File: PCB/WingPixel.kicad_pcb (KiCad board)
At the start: 4 copper layers, 50.8 x 22.9 mm, 20 parts, among them J1 Barrel_Jack, J2 Screw_Terminal_01x04, J3 Conn_01x16, J4 Conn_01x12, J5 TriSolderJumper, J6 Conn_01x02, SW1 SW_Push, U1 WingPixel, U2 LSF0102DCUR

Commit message: Changing power distribution
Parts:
- moved J5 8.24 mm to (51.1, 38.9)
- moved J6 3.84 mm to (49.5, 35.3), turned to 90 degrees
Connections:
- C1 pad 1: VEXT -> VLED
- J2 pad 1: VEXT -> VLED
- J5 pad 2: VEXT -> VLED
- R1 pad 2: VEXT -> VLED
- R4 pad 2: VEXT -> VLED
- R5 pad 2: VEXT -> VLED
- U2 pad 7: VEXT -> VLED
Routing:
- net VEXT: track 54.4 -> 7.84 mm, vias 3 -> 0
- net VUSB: track 17.8 -> 2.54 mm, vias 1 -> 0
- net VLED: track 0.00 -> 12.9 mm
- net VBATT: track 6.61 -> 2.54 mm
- removed copper zone on In1.Cu, net VEXT

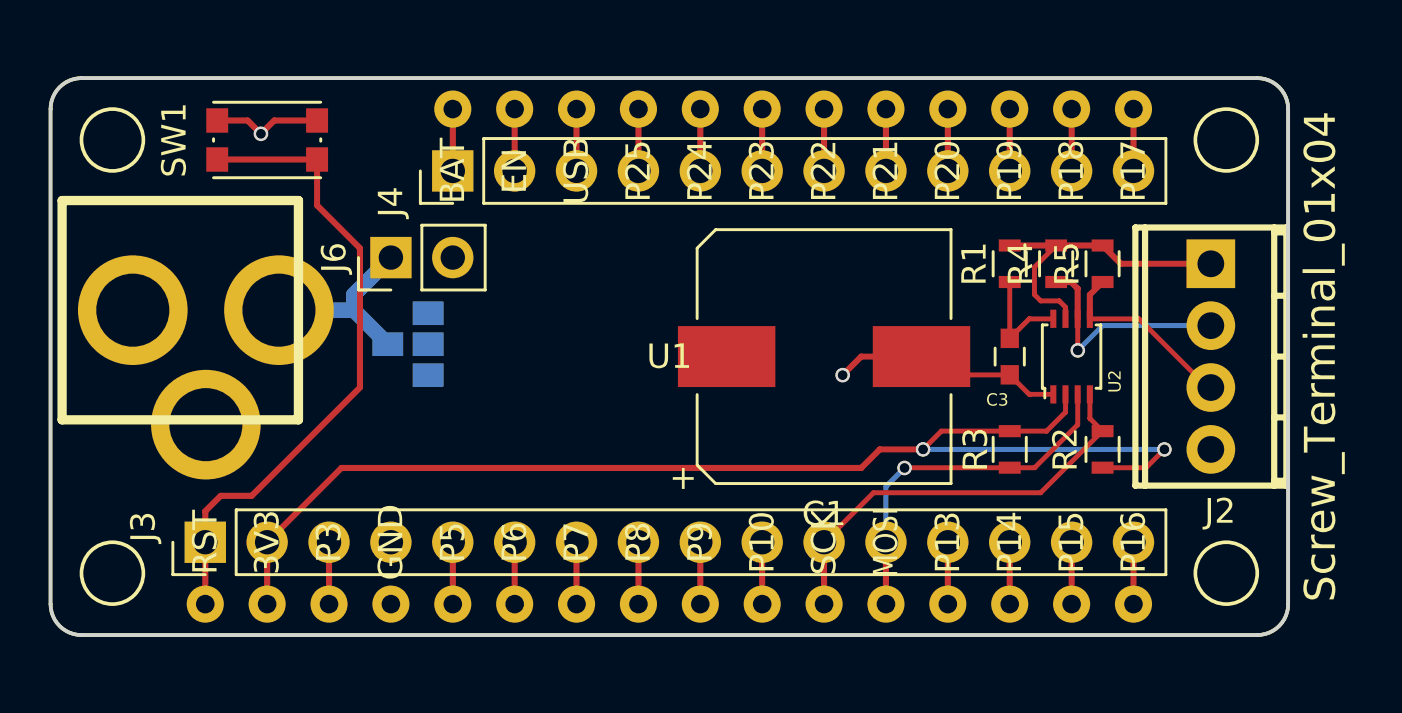
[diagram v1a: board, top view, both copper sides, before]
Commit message: Adjusted Power Distribution, defined zones
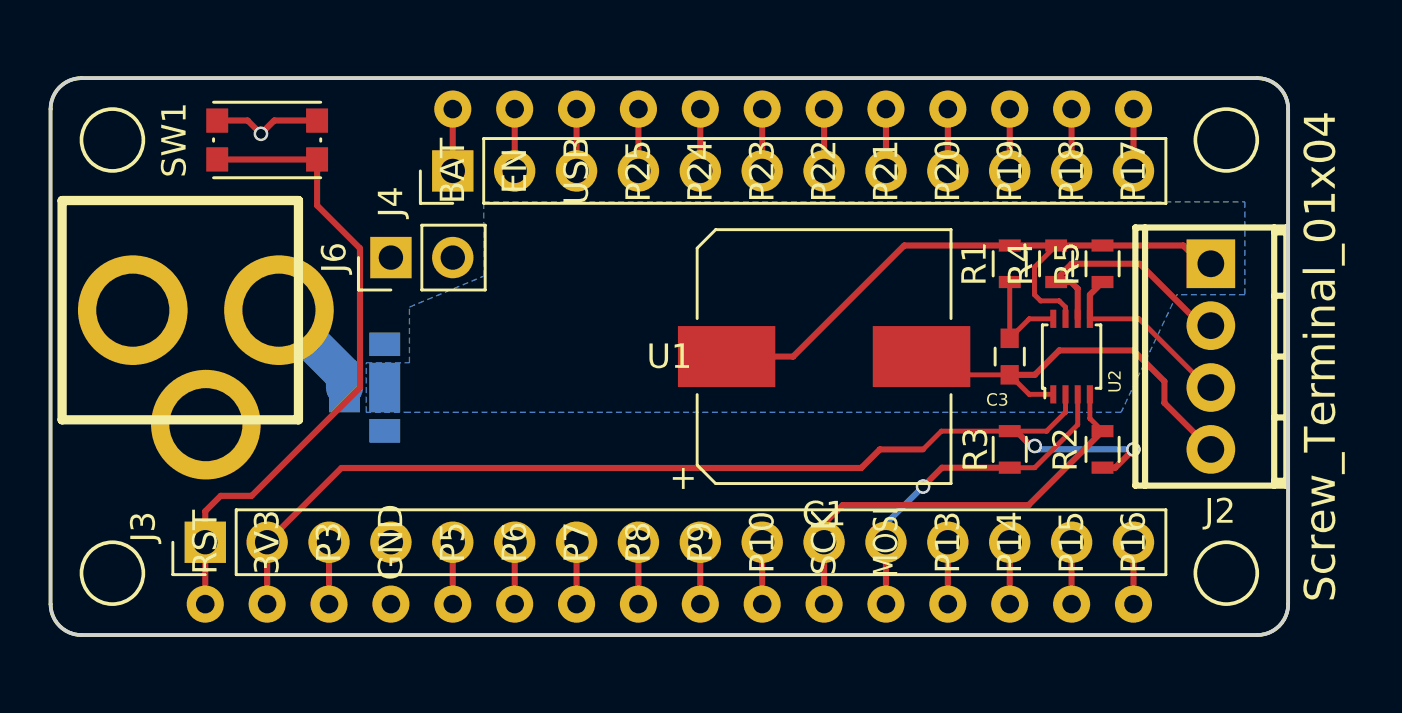
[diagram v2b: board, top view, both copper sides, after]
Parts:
- J5: footprint TriSelectSolderJumper:TriSelectSolderJumper_CutTrace -> TriSelectSolderJumper:TriSelectSolderJumper_HighCurrent
- moved J5 2.51 mm to (49.3, 40.6)
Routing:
- net GND: track 59.4 -> 39.4 mm, vias 2 -> 1
- net VLED: track 12.9 -> 26.4 mm
- net V3v3: track 51.0 -> 45.2 mm
- net VEXT: track 7.84 -> 4.29 mm
- net MOSI: track 15.0 -> 14.1 mm
- net DATA: track 9.42 -> 10.0 mm, vias 1 -> 0
- added copper zone on B.Cu, net VLED

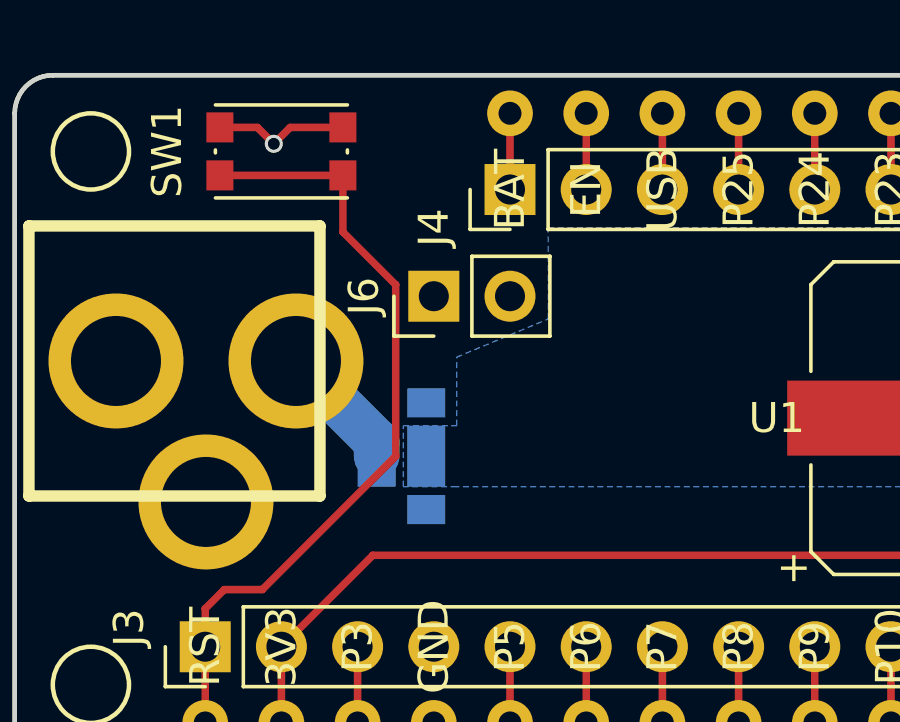
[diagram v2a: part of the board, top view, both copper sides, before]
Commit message: Connected VUSB, VBATT, Modified Zone for VEXT
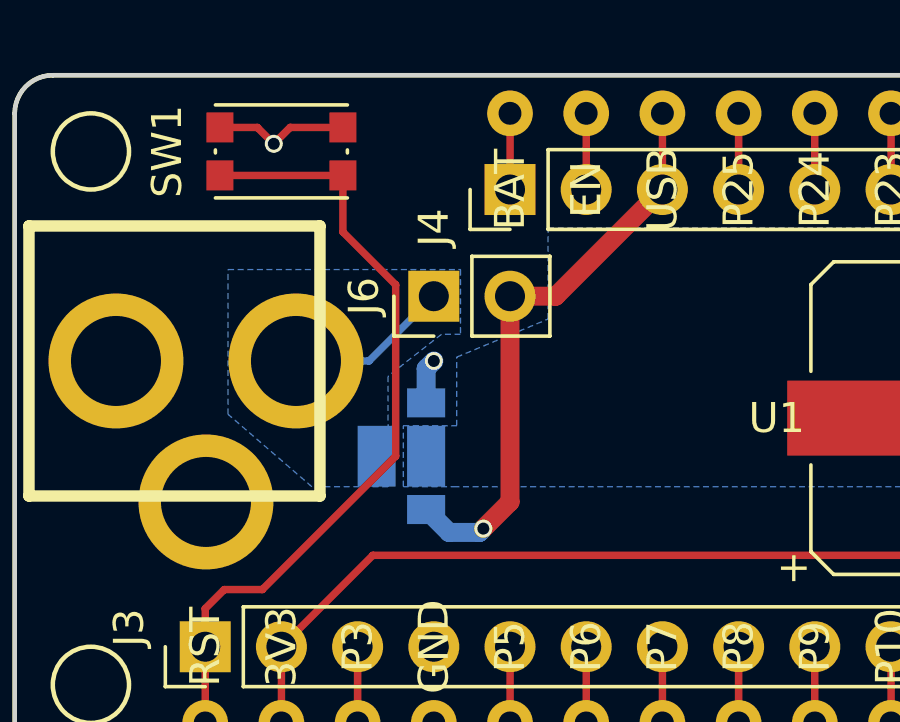
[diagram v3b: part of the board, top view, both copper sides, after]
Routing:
- net VUSB: track 2.54 -> 19.5 mm, vias 0 -> 1
- net VBATT: track 2.54 -> 13.8 mm, vias 0 -> 1
- net VEXT: track 4.29 -> 5.49 mm
- added copper zone on B.Cu, net VEXT
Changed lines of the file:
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@@
   (general
     (links 62)
-    (no_connects 5)
-    (area 35.484999 27.864999 86.435001 50.875001)
+    (no_connects 1)
+    (area 29.971429 25.695 91.948572 52.835)
     (thickness 1.6)
     (drawings 8)
-    (tracks 119)
+    (tracks 135)
     (zones 0)
     (modules 20)
@@
     (user_trace_width 0.2032)
     (user_trace_width 0.635)
-    (user_trace_width 1.524)
+    (user_trace_width 1.27)
     (trace_clearance 0.2)
-    (zone_clearance 0.381)
+    (zone_clearance 0.254)
     (zone_45_only no)
     (trace_min 0.2)
@@
   (segment (start 76.72 37.82) (end 75.73 37.82) (width 0.2032) (layer F.Cu) (net 22))
   (segment (start 75.73 37.82) (end 74.93 38.62) (width 0.2032) (layer F.Cu) (net 22))
-  (segment (start 74.93 40.12) (end 75.958 40.12) (width 0.25) (layer F.Cu) (net 23) (status 400000))
-  (segment (start 81.28 41.275) (end 83.185 43.18) (width 0.25) (layer F.Cu) (net 23) (status 800000))
+  (segment (start 74.93 40.12) (end 75.958 40.12) (width 0.25) (layer F.Cu) (net 23))
+  (segment (start 81.28 41.275) (end 83.185 43.18) (width 0.25) (layer F.Cu) (net 23))
   (segment (start 81.28 40.386) (end 81.28 41.275) (width 0.25) (layer F.Cu) (net 23))
   (segment (start 80.01 39.116) (end 81.28 40.386) (width 0.25) (layer F.Cu) (net 23))
@@
   (segment (start 76.442 42.43) (end 74.93 42.43) (width 0.2032) (layer F.Cu) (net 24))
   (segment (start 77.22 41.652) (end 76.442 42.43) (width 0.2032) (layer F.Cu) (net 24))
-  (segment (start 47.625 40.64) (end 47.625 40.15486) (width 1.524) (layer B.Cu) (net 25))
-  (segment (start 47.625 40.15486) (end 44.93514 37.465) (width 1.524) (layer B.Cu) (net 25))
+  (segment (start 44.93514 37.465) (end 47.371 37.465) (width 0.25) (layer B.Cu) (net 25))
+  (segment (start 47.371 37.465) (end 49.53 35.306) (width 0.25) (layer B.Cu) (net 25))
   (segment (start 76.835 36.31) (end 76.835 36.195) (width 0.25) (layer F.Cu) (net 26))
   (segment (start 76.835 36.195) (end 77.47 35.56) (width 0.25) (layer F.Cu) (net 26))
@@
   (segment (start 75.958 43.93) (end 74.93 43.93) (width 0.2032) (layer F.Cu) (net 30))
   (segment (start 77.72 42.168) (end 75.958 43.93) (width 0.2032) (layer F.Cu) (net 30))
+  (segment (start 52.07 31.75) (end 52.07 33.02) (width 0.635) (layer In1.Cu) (net 31))
+  (segment (start 49.276 37.719) (end 49.276 38.862) (width 0.635) (layer B.Cu) (net 31))
+  (segment (start 49.53 37.465) (end 49.276 37.719) (width 0.635) (layer B.Cu) (net 31))
+  (via (at 49.53 37.465) (size 0.6) (drill 0.4) (layers F.Cu B.Cu) (net 31))
+  (segment (start 52.324 37.465) (end 49.53 37.465) (width 0.635) (layer In1.Cu) (net 31))
+  (segment (start 53.721 36.068) (end 52.324 37.465) (width 0.635) (layer In1.Cu) (net 31))
+  (segment (start 53.721 34.671) (end 53.721 36.068) (width 0.635) (layer In1.Cu) (net 31))
+  (segment (start 52.07 33.02) (end 53.721 34.671) (width 0.635) (layer In1.Cu) (net 31))
   (segment (start 52.07 31.75) (end 52.07 29.21) (width 0.25) (layer F.Cu) (net 31))
+  (segment (start 52.07 35.306) (end 52.07 42.164) (width 0.635) (layer F.Cu) (net 32))
+  (segment (start 50.038 43.18) (end 49.276 42.418) (width 0.635) (layer B.Cu) (net 32))
+  (segment (start 51.054 43.18) (end 50.038 43.18) (width 0.635) (layer B.Cu) (net 32))
+  (segment (start 51.181 43.053) (end 51.054 43.18) (width 0.635) (layer B.Cu) (net 32))
+  (via (at 51.181 43.053) (size 0.6) (drill 0.4) (layers F.Cu B.Cu) (net 32))
+  (segment (start 52.07 42.164) (end 51.181 43.053) (width 0.635) (layer F.Cu) (net 32))
+  (segment (start 52.07 35.306) (end 53.594 35.306) (width 0.635) (layer F.Cu) (net 32))
+  (segment (start 53.594 35.306) (end 57.15 31.75) (width 0.635) (layer F.Cu) (net 32))
   (segment (start 57.15 29.21) (end 57.15 31.75) (width 0.25) (layer F.Cu) (net 32))
   (segment (start 63.31 39.37) (end 66.04 39.37) (width 0.25) (layer F.Cu) (net 33))
@@
       )
     )
+  )
+  (zone (net 25) (net_name VEXT) (layer B.Cu) (hatch edge 0.508)
+    (connect_pads (clearance 0.254))
+    (min_thickness 0.254)
+    (fill yes (arc_segments 16) (thermal_gap 0.2032) (thermal_bridge_width 1.524))
+    (polygon
+      (pts
+        (xy 50.419 36.576) (xy 49.784 36.576) (xy 48.006 37.973) (xy 48.006 41.656) (xy 45.466 41.656)
+        (xy 42.672 39.243) (xy 42.672 34.417) (xy 50.419 34.417)
+      )
+    )

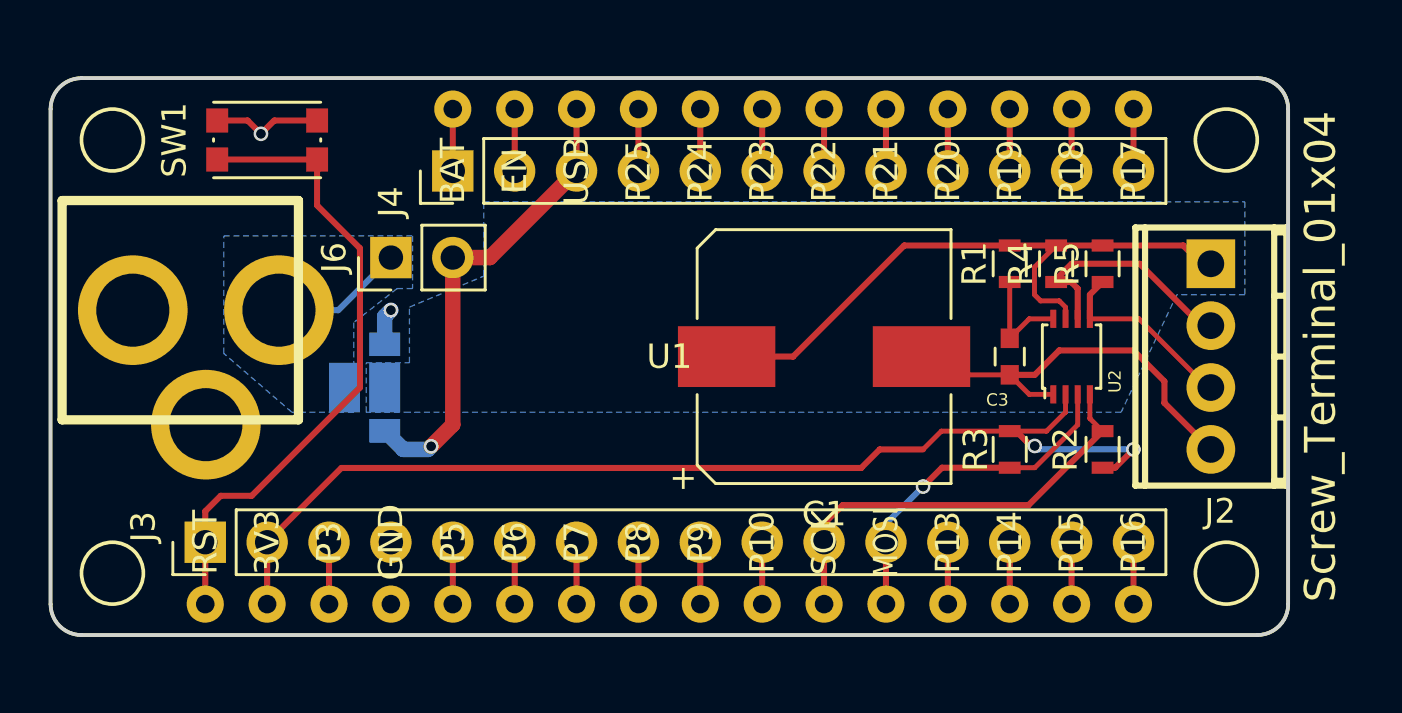
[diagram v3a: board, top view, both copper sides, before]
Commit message: Cleaned up Silk Screen, Added Labels and Logos
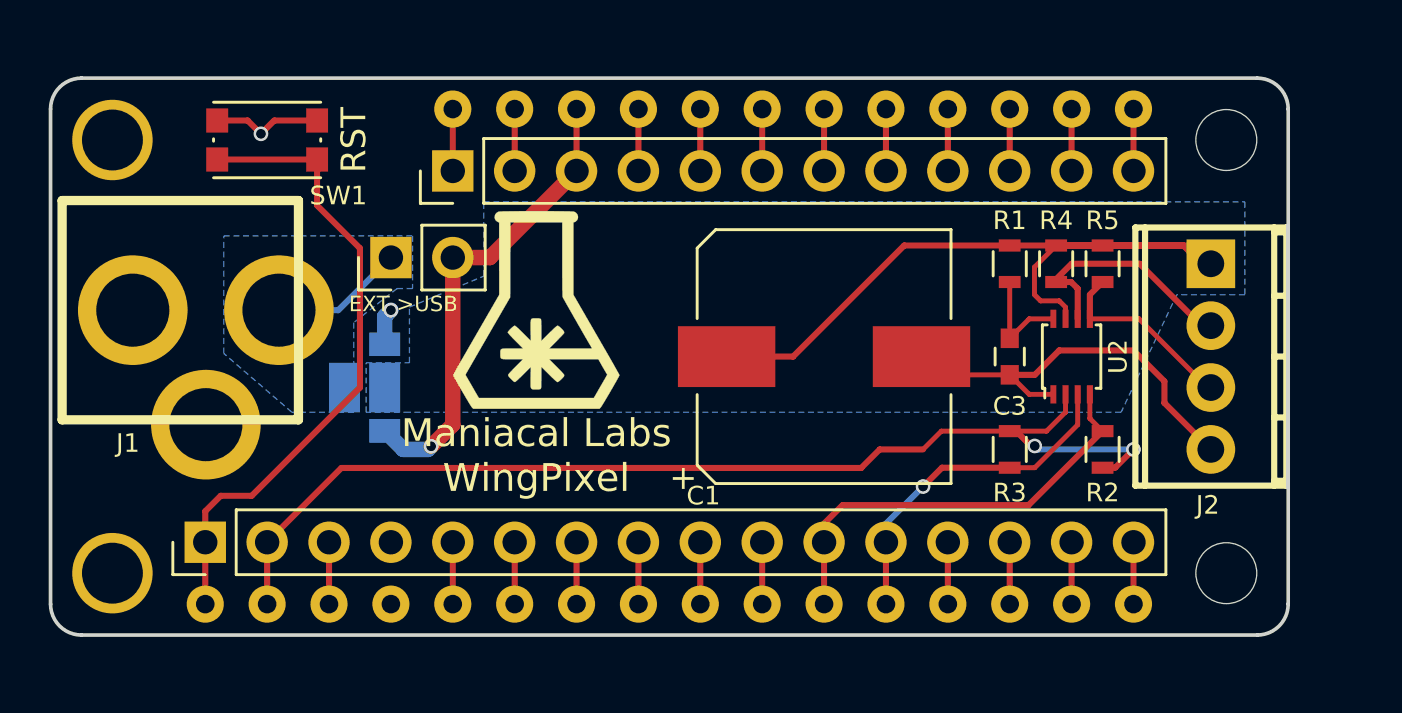
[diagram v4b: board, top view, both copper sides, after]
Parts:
- added G***: LOGO, LOGOS:logo_MLlabs_small, F.Cu at (55.5, 37.5)
- U1: footprint FeatherWing:FeatherWing -> FeatherWing:FeatherWing_NoOutline
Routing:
- net VLED: track 26.4 -> 33.1 mm
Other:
- board text added: "BAT"
- board text added: "EXT"
- board text added: "EXT >USB"
- board text added: "LED"
- board text added: "Maniacal Labs WingPixel"
- board text added: "RST"
- board text added: "USB"
- board text added: "VLED Jumper See Manual CHOOSE ONLY ONE TO POWER LEDs"

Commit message: Converted to 2-Layer board(!)
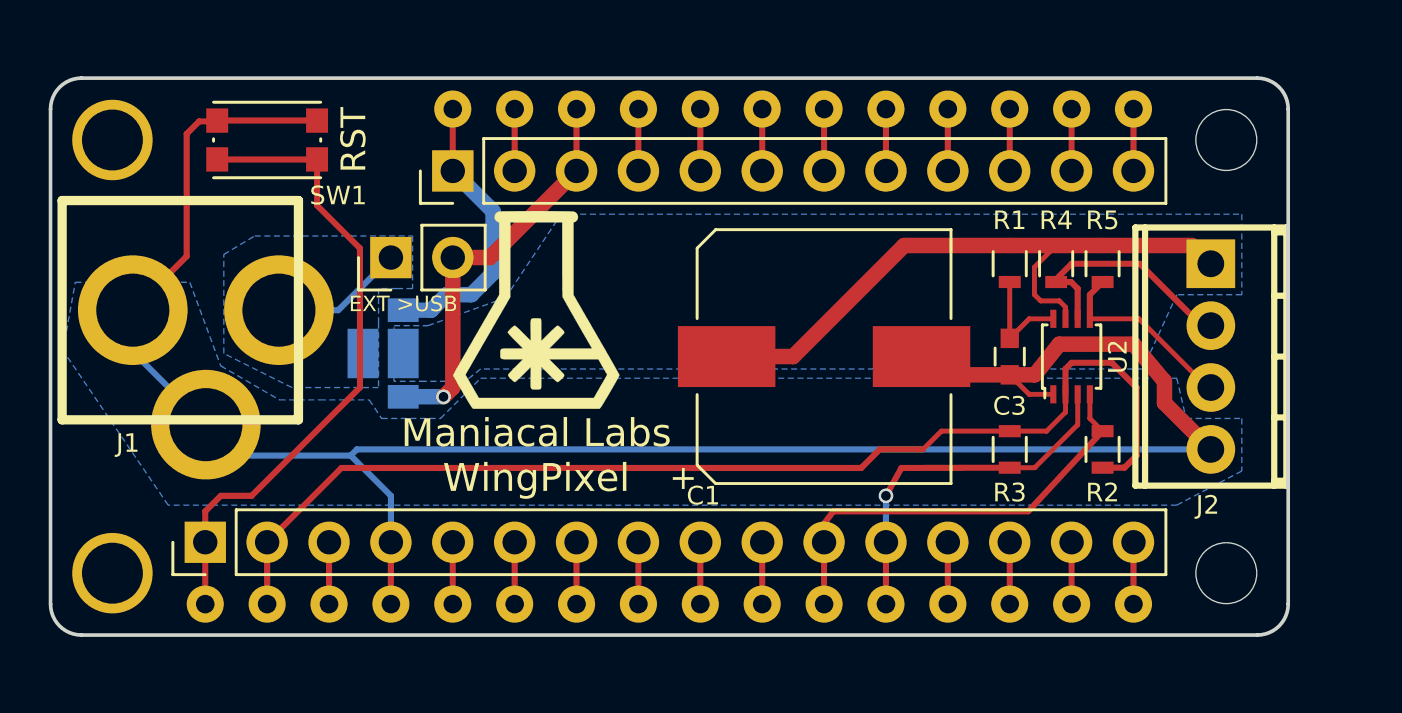
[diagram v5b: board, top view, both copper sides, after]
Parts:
- moved J5 1.59 mm to (50.0, 39.2)
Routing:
- net GND: track 39.4 -> 85.6 mm, vias 1 -> 0
- net VUSB: track 19.5 -> 16.6 mm
- net V3v3: track 45.2 -> 47.4 mm, vias 2 -> 0
- net VBATT: track 13.8 -> 11.7 mm, vias 1 -> 0
- net MOSI: track 14.1 -> 15.0 mm
- added copper zone on B.Cu, net GND
- removed copper zone on In2.Cu, net GND
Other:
- copper layers 4 -> 2
